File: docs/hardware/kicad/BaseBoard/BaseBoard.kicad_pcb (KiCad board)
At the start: 2 copper layers, 60 x 80 mm, 29 parts, among them J1 FTP cable, J2 5V in, U1 ESP32 DevKit V1, U2 BMP280 0x76

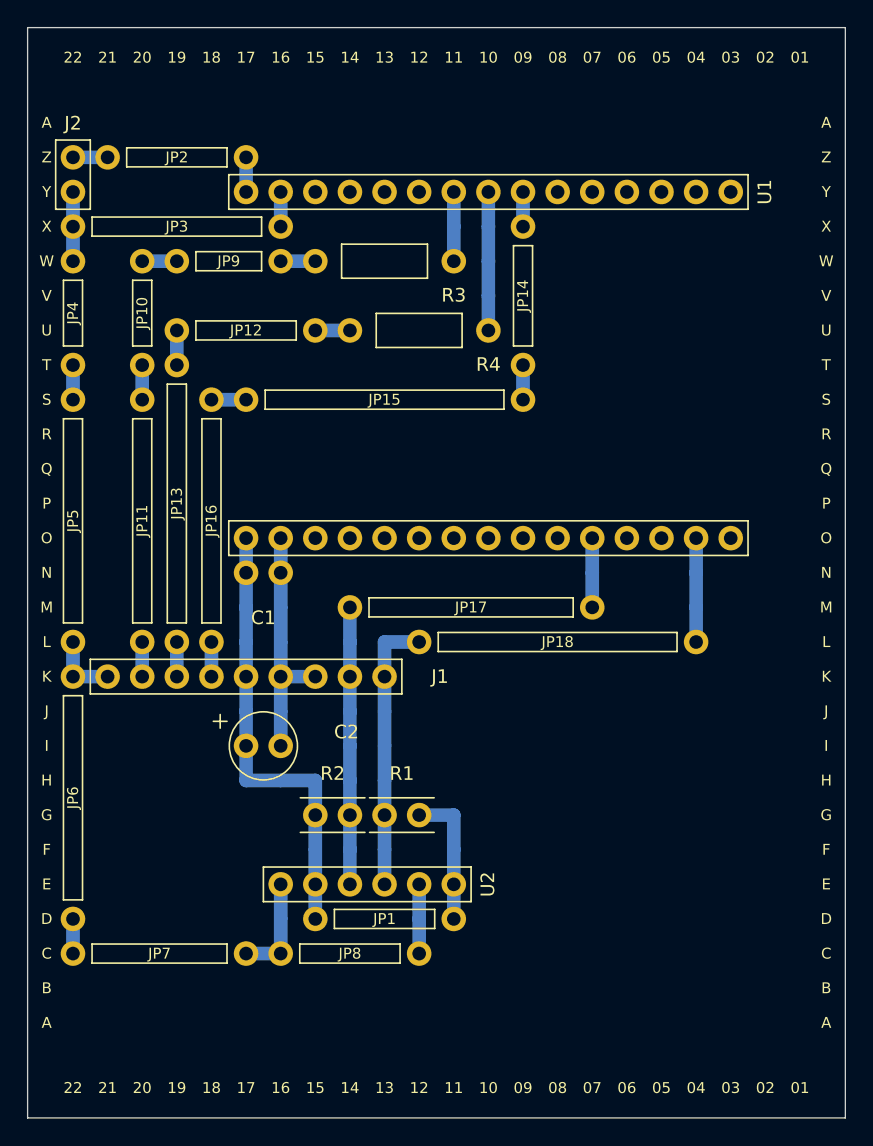
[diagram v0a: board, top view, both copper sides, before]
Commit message: feat(kicad): SPS30 UART header on the base board, runs as solder bridges
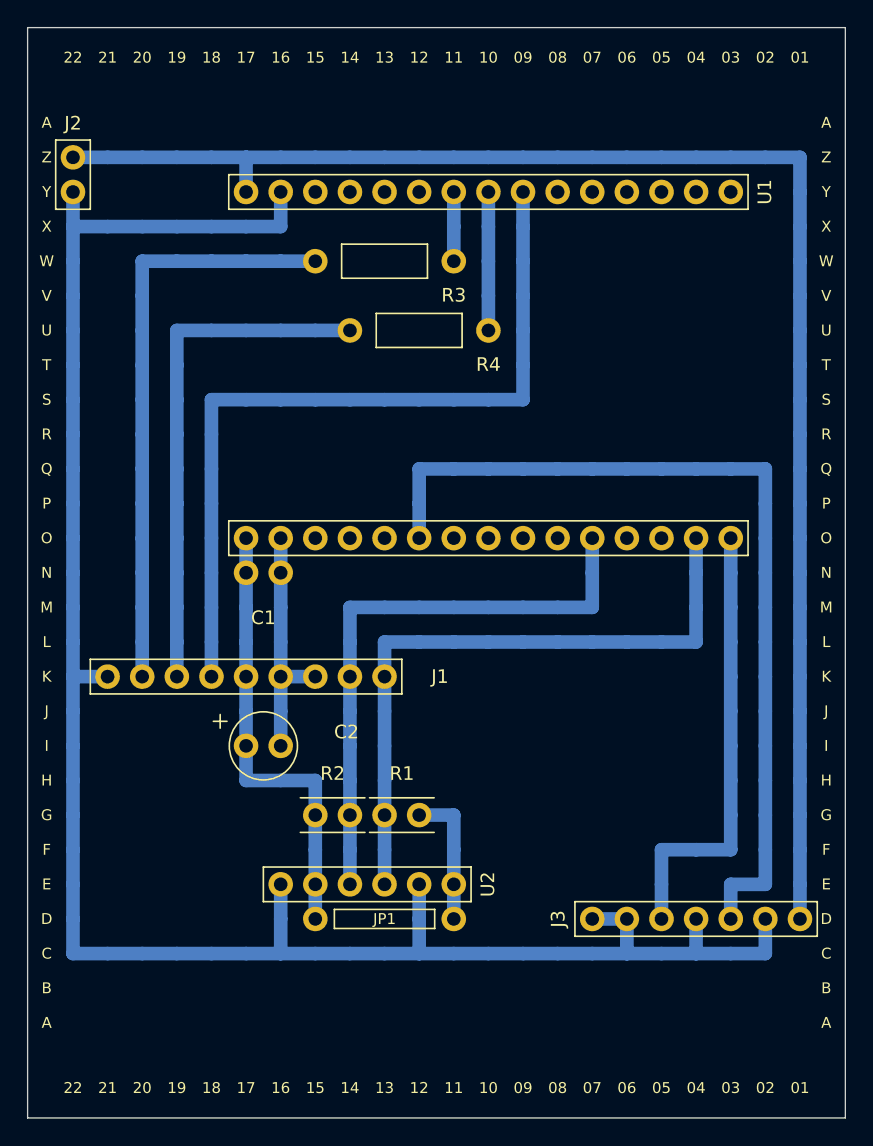
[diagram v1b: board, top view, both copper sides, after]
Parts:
- removed JP10, JP4, JP9: 0R, BaseBoard:R_Jumper_P7.62
- removed JP11, JP16, JP17, JP5, JP6: 0R, BaseBoard:R_Jumper_P17.78
- removed JP12, JP14, JP2, JP8: 0R, BaseBoard:R_Jumper_P10.16
- removed JP13, JP15, JP18: 0R, BaseBoard:R_Jumper_P20.32
- removed JP3: 0R, BaseBoard:R_Jumper_P15.24
- removed JP7: 0R, BaseBoard:R_Jumper_P12.70
- added J3: SPS30 cable, BaseBoard:PinHeader_1x07, F.Cu at (141.4, 165.4)
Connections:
- U1 pad 21: (no net) -> /SPS_TX
- U1 pad 30: (no net) -> /SPS_RX
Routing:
- net GND: track 48.3 -> 165.1 mm
- net +5V: track 5.08 -> 111.8 mm
- net /SPS_TX: track 0.00 -> 66.0 mm
- net /SD: track 10.2 -> 58.4 mm
- net /SPS_RX: track 0.00 -> 33.0 mm
- net /SCK_CABLE: track 10.2 -> 43.2 mm
- net /WS_CABLE: track 7.62 -> 38.1 mm
- net /SCL: track 27.9 -> 48.3 mm
- net /SDA: track 25.4 -> 43.2 mm
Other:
- board text added: "J3 D07-D01: drain GND RX GND TX GND 5V (SPS30 side), drain bridged to GND."
- board text added: "JP1 = 0R link on the component side, body flat on the board, where 3V3 crosses GND."
- board text added: "SPS30 UART2: GPIO23 -> sensor RX, sensor TX -> GPIO16."
- board text removed: "JP* = 0R links on the component side, body flat on the board."
